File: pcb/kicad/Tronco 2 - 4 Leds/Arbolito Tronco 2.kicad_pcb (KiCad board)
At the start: 2 copper layers, 68.2 x 111 mm, 24 parts, among them U1 WS2812B, U2 WS2812B, U3 WS2812B, U4 WS2812B

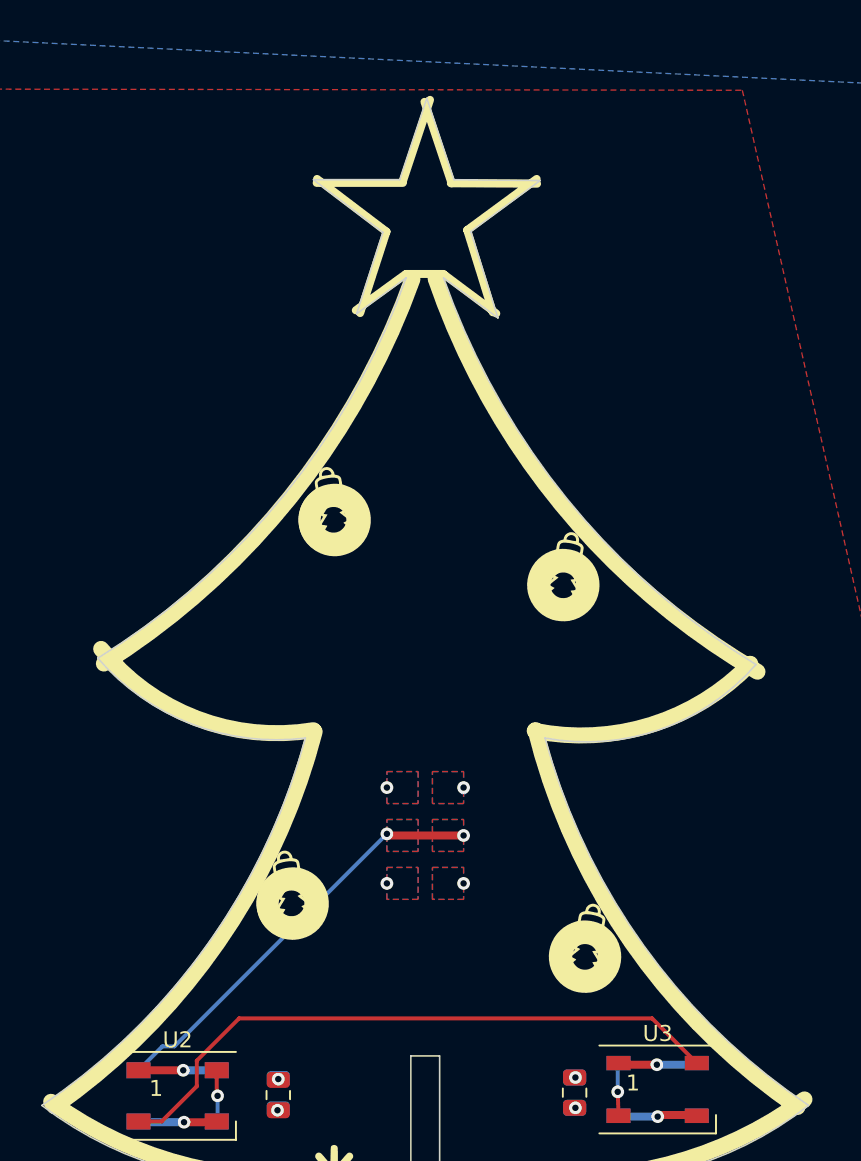
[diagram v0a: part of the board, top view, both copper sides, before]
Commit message: Footprints corrected
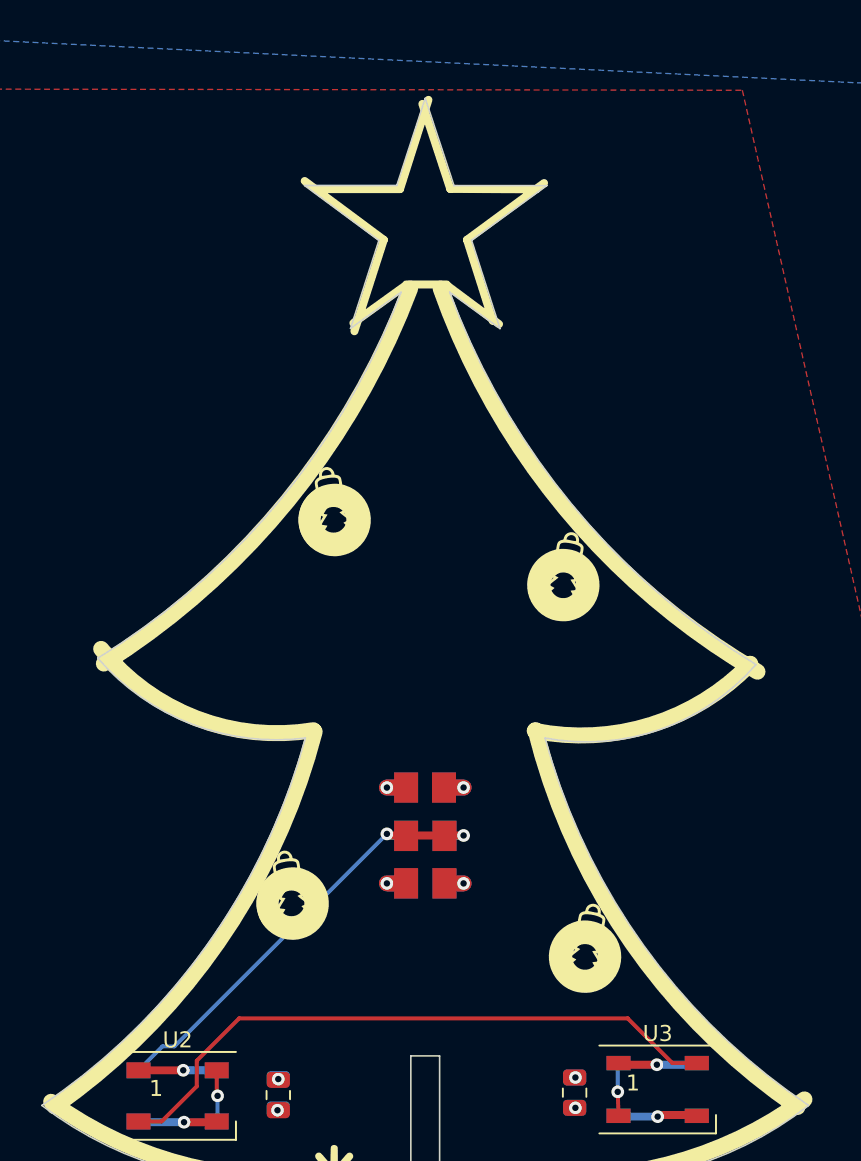
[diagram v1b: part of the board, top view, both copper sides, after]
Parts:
- added J1: Conn_01x01, Library:Output, F.Cu at (138.3, 65.1)
- added J2: Conn_01x01, Library:Output, F.Cu at (140.7, 65.1)
- added J3: Conn_01x01, Library:Output, F.Cu at (138.3, 62.1)
- added J4: Conn_01x01, Library:Output, F.Cu at (140.7, 62.1)
- added J5: Conn_01x01, Library:Output, F.Cu at (140.7, 68.1)
- added J6: Conn_01x01, Library:Output, F.Cu at (138.3, 68.1)
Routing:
- net +5V: track 9.90 -> 14.8 mm
- net GND: track 9.57 -> 14.4 mm
- net /DIN: track 26.5 -> 29.0 mm
- removed copper zone on B.Cu, net +5V
- removed copper zone on B.Cu, net /DIN
- removed copper zone on F.Cu, net /DIN
- removed copper zone on F.Cu, net GND
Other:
- outline, holes or cut-outs redrawn

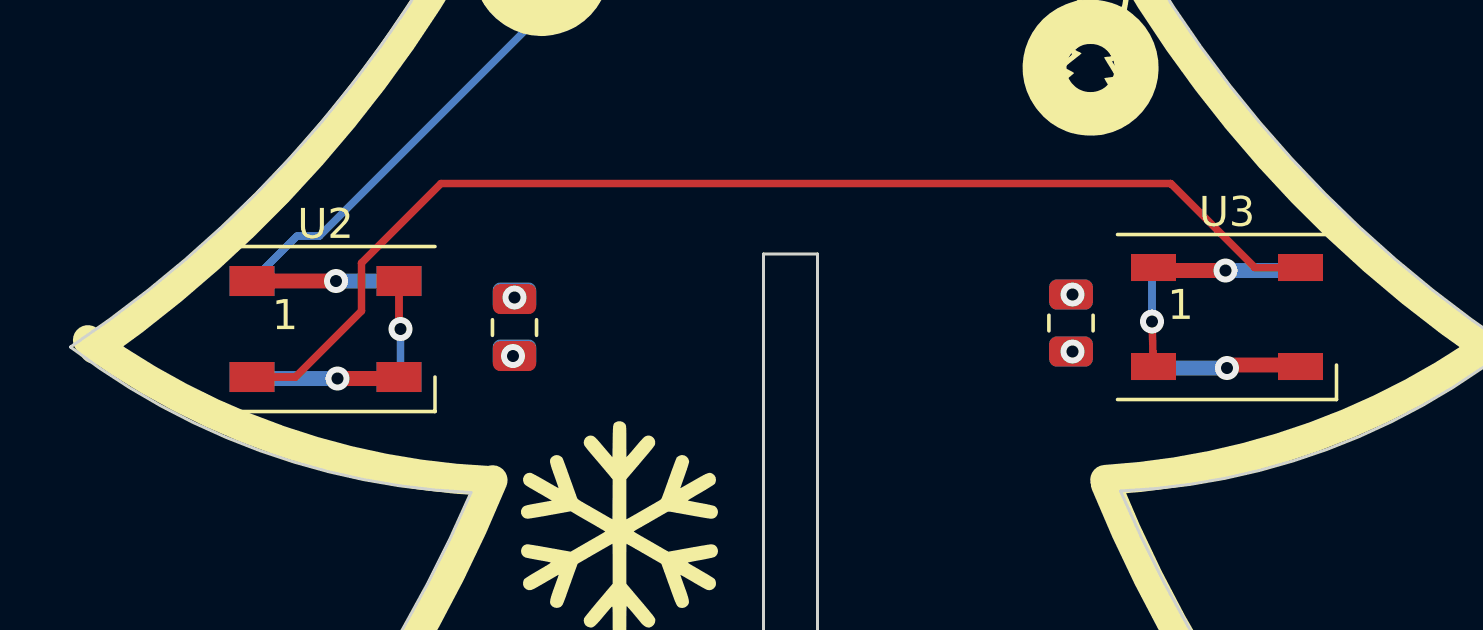
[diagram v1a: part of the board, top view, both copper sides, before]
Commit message: Led Footprint Changed
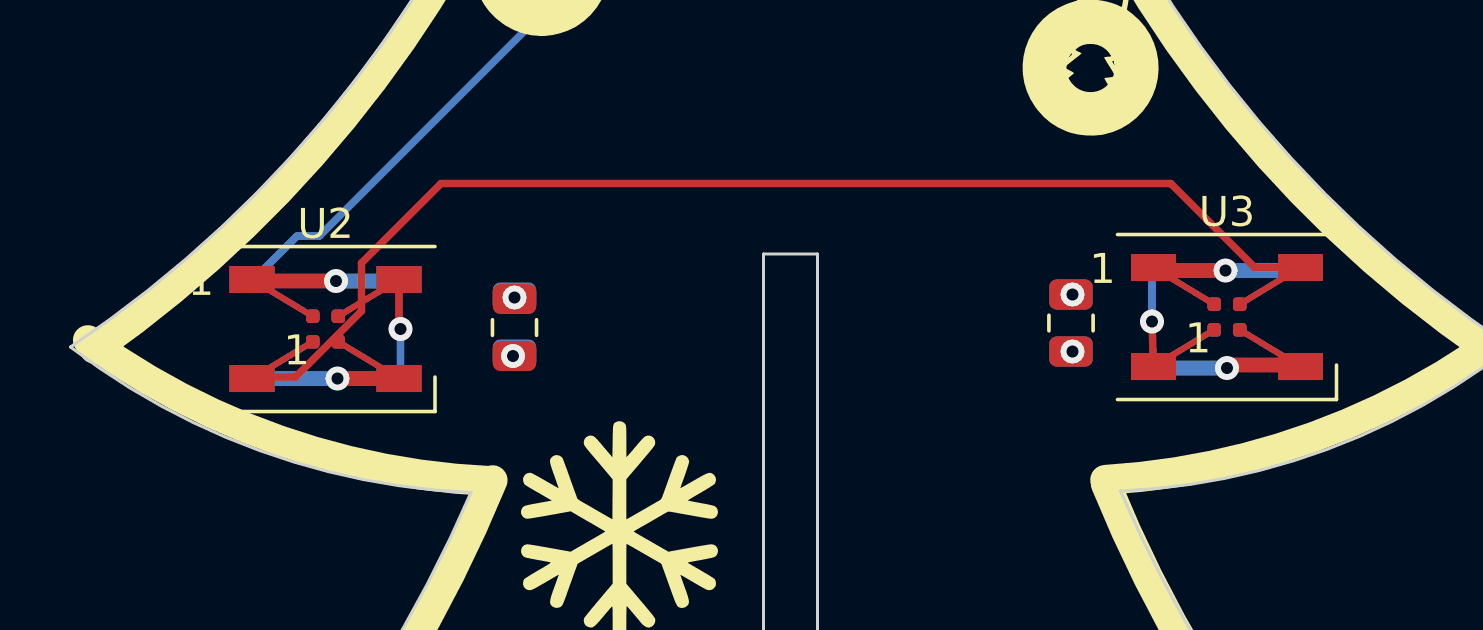
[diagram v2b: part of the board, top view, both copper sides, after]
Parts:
- U1, U2, U3, U4: footprint LED_SMD:LED_WS2812B_PLCC4_5.0x5.0mm_P3.2mm -> Library:LED_WS2812B_PLCC4_5.0x5.0mm_P3.2mm
